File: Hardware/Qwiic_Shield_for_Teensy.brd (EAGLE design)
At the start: 17.8 x 35.6 mm, 38 parts, among them J1 TEENSY, J2 QWIIC_RA, J3 QWIIC_RA, J4 QWIIC_Vertical, J5 QWIIC_Vertical, J6 ALT PWR

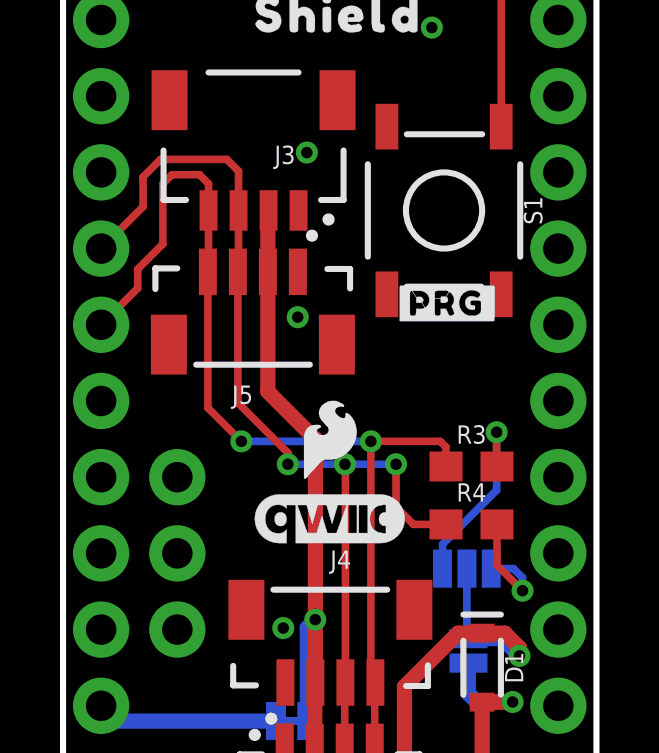
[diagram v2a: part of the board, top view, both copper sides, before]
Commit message: checklist run post design review
-approved DRC overlap and clearance errors.
-one small trace nudge to remove one extra unecessary kink
-part name text adjustments for assembly sheet
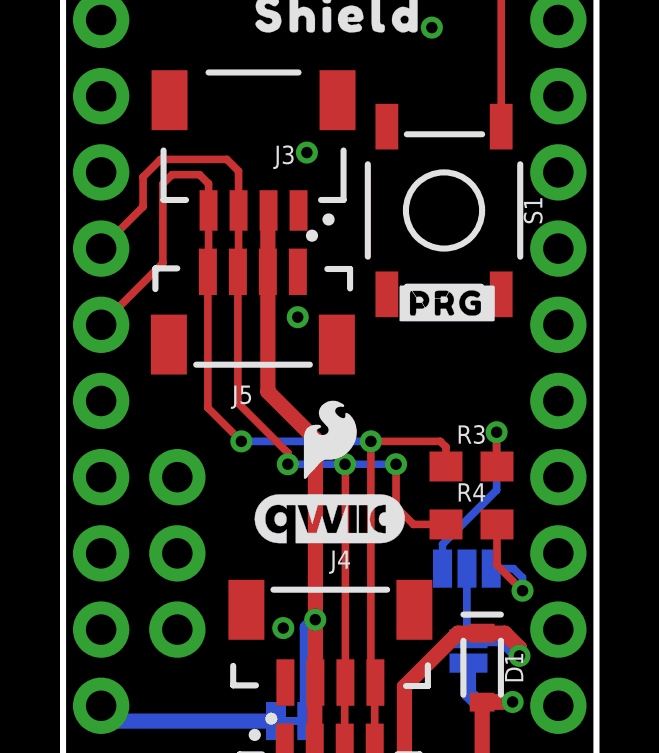
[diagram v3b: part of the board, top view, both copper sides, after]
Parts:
- S1: value (none) -> SMD_5.2MM
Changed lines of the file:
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@@
 <layer number="27" name="tValues" color="7" fill="1" visible="no" active="yes"/>
 <layer number="28" name="bValues" color="7" fill="1" visible="no" active="yes"/>
-<layer number="29" name="tStop" color="7" fill="3" visible="yes" active="yes"/>
+<layer number="29" name="tStop" color="7" fill="3" visible="no" active="yes"/>
 <layer number="30" name="bStop" color="7" fill="6" visible="no" active="yes"/>
 <layer number="31" name="tCream" color="7" fill="4" visible="no" active="yes"/>
@@
 <layer number="45" name="Holes" color="7" fill="1" visible="yes" active="yes"/>
 <layer number="46" name="Milling" color="3" fill="1" visible="no" active="yes"/>
-<layer number="47" name="Measures" color="7" fill="1" visible="yes" active="yes"/>
+<layer number="47" name="Measures" color="7" fill="1" visible="no" active="yes"/>
 <layer number="48" name="Document" color="7" fill="1" visible="no" active="yes"/>
 <layer number="49" name="Reference" color="7" fill="1" visible="yes" active="yes"/>
@@
 <attribute name="NAME" x="7.493" y="2.921" size="0.6096" layer="25" font="vector" ratio="20"/>
 <attribute name="PROD_ID" value="CONN-13694" x="8.89" y="5.08" size="1.778" layer="27" display="off"/>
-<attribute name="VALUE" x="7.239" y="1.778" size="0.6096" layer="27" font="vector" ratio="20"/>
+<attribute name="VALUE" x="7.0104" y="0.7874" size="0.6096" layer="27" font="vector" ratio="20"/>
 </element>
 <element name="J3" library="SparkFun-Connectors" package="JST04_1MM_RA" value="QWIIC_RA" x="6.35" y="22.86" smashed="yes" rot="R180">
 <attribute name="NAME" x="7.747" y="25.019" size="0.6096" layer="25" font="vector" ratio="20" rot="R180"/>
 <attribute name="PROD_ID" value="CONN-13694" x="6.35" y="22.86" size="1.778" layer="27" rot="R180" display="off"/>
-<attribute name="VALUE" x="8.001" y="26.162" size="0.6096" layer="27" font="vector" ratio="20" rot="R180"/>
+<attribute name="VALUE" x="8.3312" y="27.178" size="0.6096" layer="27" font="vector" ratio="20" rot="R180"/>
 </element>
 <element name="J5" library="SparkFun-Connectors" package="JST04_1MM_VERT" value="QWIIC_Vertical" x="6.35" y="21.59" smashed="yes" rot="R180">
 <attribute name="NAME" x="6.334" y="17.02366875" size="0.6096" layer="25" rot="R180"/>
 <attribute name="PROD_ID" value="CONN-14483" x="6.35" y="21.59" size="1.778" layer="27" rot="R180" display="off"/>
-<attribute name="VALUE" x="6.334" y="22.88633125" size="0.6096" layer="27" rot="R180"/>
+<attribute name="VALUE" x="9.2042" y="17.24753125" size="0.6096" layer="27" font="vector" ratio="20" rot="R180"/>
 </element>
 <element name="LOGO1" library="SparkFun-Aesthetics" package="SFE_LOGO_NAME_FLAME_.1" value="SFE_LOGO_NAME_FLAME.1_INCH" x="8.9408" y="28.829" smashed="yes" rot="MR0"/>
@@
 <attribute name="NAME" x="13.6144" y="15.0876" size="0.6096" layer="25" font="vector" ratio="20" align="bottom-center"/>
 <attribute name="PROD_ID" value="RES-07857" x="13.6144" y="19.4056" size="1.778" layer="27" display="off"/>
-<attribute name="VALUE" x="13.6144" y="13.5636" size="0.6096" layer="27" font="vector" ratio="20" align="top-center"/>
+<attribute name="VALUE" x="13.6144" y="15.621" size="0.6096" layer="27" font="vector" ratio="20" align="top-center"/>
 </element>
 <element name="R4" library="SparkFun-Resistors" package="0603" value="4.7k" x="13.6144" y="12.3952" smashed="yes">
 <attribute name="NAME" x="13.6144" y="13.1572" size="0.6096" layer="25" font="vector" ratio="20" align="bottom-center"/>
 <attribute name="PROD_ID" value="RES-07857" x="9.8044" y="13.6652" size="1.778" layer="27" display="off"/>
-<attribute name="VALUE" x="13.6144" y="11.6332" size="0.6096" layer="27" font="vector" ratio="20" align="top-center"/>
+<attribute name="VALUE" x="13.6652" y="13.6398" size="0.6096" layer="27" font="vector" ratio="20" align="top-center"/>
 </element>
 <element name="I2C" library="SparkFun-Jumpers" package="SMT-JUMPER_3_NO_SILK" package3d_urn="urn:adsk.eagle:package:39285/1" value="JUMPER-SMT_3_NO_SILK" x="13.462" y="10.922" smashed="yes" rot="MR180">
@@
 <attribute name="NAME" x="8.906" y="10.91633125" size="0.6096" layer="25"/>
 <attribute name="PROD_ID" value="CONN-14483" x="0" y="15.24" size="1.778" layer="27" font="vector" ratio="15" display="off"/>
-<attribute name="VALUE" x="8.906" y="5.05366875" size="0.6096" layer="27"/>
+<attribute name="VALUE" x="6.0612" y="10.69246875" size="0.6096" layer="27" font="vector" ratio="20"/>
 </element>
 <element name="U$15" library="output" package="#3V3#0" value="" x="5.9182" y="6.3754" smashed="yes" rot="MR0"/>
@@
 <element name="J6" library="SparkFun-Connectors" package="1X02_NO_SILK" value="ALT PWR" x="13.97" y="1.27" smashed="yes" rot="R90">
 <attribute name="NAME" x="12.573" y="0" size="0.6096" layer="25" font="vector" ratio="20" rot="R90"/>
-<attribute name="VALUE" x="16.002" y="0" size="0.6096" layer="27" font="vector" ratio="20" rot="R90"/>
+<attribute name="VALUE" x="15.5448" y="0.5842" size="0.6096" layer="27" font="vector" ratio="20" rot="R90"/>
 </element>
 <element name="3V3_ISO" library="SparkFun-Jumpers" package="SMT-JUMPER_2_NC_TRACE_SILK" package3d_urn="urn:adsk.eagle:package:39281/1" value="" x="7.62" y="5.842" smashed="yes" rot="MR0">
@@
 <attribute name="NAME" x="14.732" y="7.62" size="0.6096" layer="25" font="vector" ratio="20" rot="R270" align="bottom-center"/>
 <attribute name="PROD_ID" value="DIO-14072" x="13.97" y="7.62" size="1.778" layer="27" rot="R270" display="off"/>
-<attribute name="VALUE" x="13.208" y="7.62" size="0.6096" layer="27" font="vector" ratio="20" rot="R270" align="top-center"/>
-</element>
-<element name="S1" library="SparkFun-Switches" package="TACTILE_SWITCH_SMD_5.2MM" value="" x="12.7" y="22.86" smashed="yes" rot="R270">
+<attribute name="VALUE" x="15.4432" y="7.6962" size="0.6096" layer="27" font="vector" ratio="20" rot="R270" align="top-center"/>
+</element>
+<element name="S1" library="SparkFun-Switches" package="TACTILE_SWITCH_SMD_5.2MM" value="SMD_5.2MM" x="12.7" y="22.86" smashed="yes" rot="R270">
 <attribute name="NAME" x="15.367" y="22.86" size="0.6096" layer="25" font="vector" ratio="20" rot="R270" align="bottom-center"/>
 <attribute name="PROD_ID" value="SWCH-14139" x="12.7" y="22.86" size="1.778" layer="27" rot="R270" display="off"/>
-<attribute name="VALUE" x="10.033" y="22.86" size="0.6096" layer="27" font="vector" ratio="20" rot="R270" align="top-center"/>
+<attribute name="VALUE" x="12.6238" y="21.59" size="0.6096" layer="27" font="vector" ratio="20" align="top-center"/>
 </element>
 <element name="U$5" library="output" package="#ALT_3V3#0" value="" x="9.525" y="3.81" smashed="yes" rot="MR0"/>
@@
 <wire x1="8.412" y1="9.2156" x2="8.4074" y2="9.2202" width="0.508" layer="1"/>
 <via x="8.4074" y="9.2202" extent="1-16" drill="0.381"/>
-<wire x1="6.858" y1="22.868" x2="6.85" y2="22.86" width="0.508" layer="1"/>
 <wire x1="6.828" y1="20.815" x2="6.828" y2="22.838" width="0.508" layer="1"/>
 <wire x1="6.828" y1="22.838" x2="6.85" y2="22.86" width="0.508" layer="1"/>
@@
 <wire x1="8.6868" y1="3.7846" x2="10.9474" y2="3.7846" width="0.508" layer="1"/>
 <wire x1="11.3792" y1="4.2164" x2="10.9474" y2="3.7846" width="0.508" layer="1"/>
-<wire x1="13.462" y1="10.922" x2="13.4874" y2="10.8966" width="0.254" layer="16"/>
 <wire x1="8.1407" y1="5.842" x2="8.1407" y2="8.9535" width="0.508" layer="16"/>
 <wire x1="8.1407" y1="8.9535" x2="8.4074" y2="9.2202" width="0.508" layer="16"/>
@@
 <wire x1="4.85" y1="22.86" x2="4.85" y2="20.837" width="0.254" layer="1"/>
 <wire x1="4.85" y1="20.837" x2="4.828" y2="20.815" width="0.254" layer="1"/>
-<wire x1="1.27" y1="19.05" x2="2.4892" y2="20.2692" width="0.254" layer="1"/>
 <wire x1="3.3274" y1="23.749" x2="3.6322" y2="24.0538" width="0.254" layer="1"/>
 <wire x1="3.6322" y1="24.0538" x2="4.5466" y2="24.0538" width="0.254" layer="1"/>
 <wire x1="4.85" y1="23.7504" x2="4.85" y2="22.86" width="0.254" layer="1"/>
-<wire x1="2.4892" y1="20.2692" x2="2.4892" y2="20.9042" width="0.254" layer="1"/>
-<wire x1="2.4892" y1="20.9042" x2="3.3274" y2="21.7424" width="0.254" layer="1"/>
-<wire x1="3.3274" y1="21.7424" x2="3.3274" y2="23.749" width="0.254" layer="1"/>
+<wire x1="1.27" y1="19.05" x2="3.3274" y2="21.1074" width="0.254" layer="1"/>
+<wire x1="3.3274" y1="21.1074" x2="3.3274" y2="23.749" width="0.254" layer="1"/>
 <wire x1="4.5466" y1="24.0538" x2="4.85" y2="23.7504" width="0.254" layer="1"/>
 <wire x1="12.7644" y1="14.3256" x2="12.7644" y2="14.9724" width="0.254" layer="1"/>
